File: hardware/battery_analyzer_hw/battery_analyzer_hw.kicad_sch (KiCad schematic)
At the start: 0 parts

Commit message: feat(hw): add USB-C with native JTAG and AMS1117-3.3 power block
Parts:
- added C1: 10uF, Package_SO:SOIC-8_3.9x4.9mm_P1.27mm, symbol Device:C_Polarized_Small
- added C2: 100nF, Package_TO_SOT_SMD:SOT-23-6, symbol Device:C_Small
- added C3: 22uF, symbol Device:C_Polarized_Small
- added C4: 100nF, symbol Device:C_Small
- added F1: Polyfuse 500mA, symbol Device:Polyfuse
- added J1: USB_C_Receptacle_USB2.0_16P, symbol Connector:USB_C_Receptacle_USB2.0_16P
- added R1: 5k1, Package_DIP:DIP-8_W7.62mm, symbol Device:R
- added R2: 5k1, symbol Device:R
- added U1: USBLC6-2SC6, Package_TO_SOT_SMD:SOT-23-6, symbol Power_Protection:USBLC6-2SC6
- added U2: AMS1117-3.3, Package_TO_SOT_SMD:SOT-223-3_TabPin2, symbol Regulator_Linear:AMS1117-3.3
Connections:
- new net: F1.2, J1.A4 (VBUS), J1.A9 (VBUS), J1.B4 (VBUS), J1.B9 (VBUS)
- new net: J1.A5 (CC1), R2.1
- new net: J1.A6 (D+), J1.B6 (D+), U1.3 (I/O2)
- new net: J1.A7 (D-), J1.B7 (D-), U1.1 (I/O1)
- new net: J1.B5 (CC2), R1.1
- new net +3.3V: C3.1, C4.1, U2.2 (VO)
- new net +5V: C1.1, C2.1, F1.1, U1.5 (VBUS), U2.3 (VI)
- new net GND: C1.2, C2.2, C3.2, C4.2, J1.A1 (GND), J1.A12 (GND), J1.B1 (GND), J1.B12 (GND), J1.SH (SHIELD), R1.2, R2.2, U1.2 (GND), U2.1 (GND)
- new net USB_D+: U1.4 (I/O2)
- new net USB_D-: U1.6 (I/O1)
- no-connect marks 0 -> 2

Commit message: feat(hw): add ESP32-S3 core, strapping pins and boot logic
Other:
- added sheet MCU_Core (mcu_core.kicad_sch)
- moved on the sheet: U1
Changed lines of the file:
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@@
 	(wire
 		(pts
-			(xy 113.03 60.96) (xy 123.19 60.96)
+			(xy 123.19 69.85) (xy 133.35 69.85)
 		)
 		(stroke
@@
 	(wire
 		(pts
-			(xy 113.03 58.42) (xy 123.19 58.42)
-		)
-		(stroke
-			(width 0)
-			(type default)
-		)
-	)
-	(wire
-		(pts
-			(xy 99.06 49.53) (xy 107.95 49.53)
+			(xy 123.19 67.31) (xy 133.35 67.31)
+		)
+		(stroke
+			(width 0)
+			(type default)
+		)
+	)
+	(wire
+		(pts
+			(xy 109.22 58.42) (xy 118.11 58.42)
 		)
 		(stroke
@@
 	(wire
 		(pts
-			(xy 76.2 55.88) (xy 76.2 58.42)
+			(xy 76.2 55.88) (xy 76.2 67.31)
 		)
 		(stroke
@@
 	(wire
 		(pts
-			(xy 72.39 60.96) (xy 102.87 60.96)
+			(xy 72.39 69.85) (xy 113.03 69.85)
 		)
 		(stroke
@@
 	(wire
 		(pts
-			(xy 76.2 58.42) (xy 102.87 58.42)
+			(xy 76.2 67.31) (xy 113.03 67.31)
 		)
 		(stroke
@@
 	(wire
 		(pts
-			(xy 107.95 49.53) (xy 107.95 53.34)
+			(xy 118.11 58.42) (xy 118.11 62.23)
 		)
 		(stroke
@@
 	(wire
 		(pts
+			(xy 72.39 69.85) (xy 72.39 60.96)
+		)
+		(stroke
+			(width 0)
+			(type default)
+		)
+	)
+	(wire
+		(pts
 			(xy 26.67 115.57) (xy 36.83 115.57)
 		)
@@
 	(wire
 		(pts
-			(xy 107.95 66.04) (xy 107.95 74.93)
+			(xy 118.11 74.93) (xy 118.11 83.82)
 		)
 		(stroke
@@
 	)
 	(label "USB_D-"
-		(at 123.19 58.42 0)
+		(at 133.35 67.31 0)
 		(effects
 			(font
@@
 	)
 	(label "+5V"
-		(at 96.52 40.64 0)
+		(at 104.14 40.64 0)
 		(effects
 			(font
@@
 	)
 	(label "USB_D+"
-		(at 123.19 60.96 0)
+		(at 133.35 69.85 0)
 		(effects
 			(font
@@
 	)
 	(label "+5V"
-		(at 31.75 115.57 0)
+		(at 26.67 115.57 0)
 		(effects
 			(font
@@
 	)
 	(label "+5V"
-		(at 99.06 49.53 0)
+		(at 109.22 58.42 0)
 		(effects
 			(font
@@
 	(symbol
 		(lib_id "power:GND")
-		(at 107.95 74.93 0)
+		(at 118.11 83.82 0)
 		(unit 1)
 		(body_style 1)
@@
 		(fields_autoplaced yes)
 		(property "Reference" "#PWR04"
-			(at 107.95 81.28 0)
+			(at 118.11 90.17 0)
 			(hide yes)
 			(show_name no)
@@
 		)
 		(property "Value" "GND"
-			(at 107.95 80.01 0)
+			(at 118.11 88.9 0)
 			(show_name no)
 			(do_not_autoplace no)
@@
 		)
 		(property "Footprint" ""
-			(at 107.95 74.93 0)
+			(at 118.11 83.82 0)
 			(hide yes)
 			(show_name no)
@@
 		)
 		(property "Datasheet" ""
-			(at 107.95 74.93 0)
+			(at 118.11 83.82 0)
 			(hide yes)
 			(show_name no)
@@
 		)
 		(property "Description" "Power symbol creates a global label with name \"GND\" , ground"
-			(at 107.95 74.93 0)
+			(at 118.11 83.82 0)
 			(hide yes)
 			(show_name no)
@@
 	(symbol
 		(lib_id "Power_Protection:USBLC6-2SC6")
-		(at 107.95 58.42 0)
+		(at 118.11 67.31 0)
 		(unit 1)
 		(body_style 1)
@@
 		(fields_autoplaced yes)
 		(property "Reference" "U1"
-			(at 109.6011 50.8 0)
+			(at 119.7611 59.69 0)
 			(show_name no)
 			(do_not_autoplace no)
@@
 		)
 		(property "Value" "USBLC6-2SC6"
-			(at 109.6011 53.34 0)
+			(at 119.7611 62.23 0)
 			(show_name no)
 			(do_not_autoplace no)
@@
 		)
 		(property "Footprint" "Package_TO_SOT_SMD:SOT-23-6"
-			(at 109.22 64.77 0)
+			(at 119.38 73.66 0)
 			(hide yes)
 			(show_name no)
@@
 		)
 		(property "Datasheet" "https://www.st.com/resource/en/datasheet/usblc6-2.pdf"
-			(at 109.22 66.675 0)
+			(at 119.38 75.565 0)
 			(hide yes)
 			(show_name no)
@@
 		)
 		(property "Description" "Very low capacitance ESD protection diode, 2 data-line, SOT-23-6"
-			(at 107.95 58.42 0)
+			(at 118.11 67.31 0)
 			(hide yes)
 			(show_name no)
@@
 				)
 			)
+		)
+	)
+	(sheet
+		(at -2.54 -257.81)
+		(size 311.15 218.44)
+		(exclude_from_sim no)
+		(in_bom yes)
+		(on_board yes)
+		(dnp no)
+		(fields_autoplaced yes)
+		(stroke
+			(width 0.1524)
+			(type solid)
+		)
+		(fill
+			(color 0 0 0 0)
+		)
+		(property "Sheetname" "MCU_Core"
+			(at -2.54 -258.5216 0)
+			(show_name no)
+			(do_not_autoplace no)
+			(effects
+				(font
+					(size 1.27 1.27)
+				)
+				(justify left bottom)
+			)
+		)
+		(property "Sheetfile" "mcu_core.kicad_sch"
+			(at -2.54 -38.7854 0)
+			(show_name no)
+			(do_not_autoplace no)
+			(effects
+				(font
+					(size 1.27 1.27)
+				)
+				(justify left top)
+			)
+		)
+		(instances
+			(project "battery_analyzer_hw"
+				(path "/1337d129-c752-45b4-85a9-21e5a5723565"
+					(page "2")
+				)
+			)

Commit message: feat(hw): add UI sheet with dual OLEDs, encoder and button
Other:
- added sheet UI_Controls (ui_controls.kicad_sch)
- moved on the sheet: C1, C2, C3, C4, F1, J1, R1, R2, U1, U2

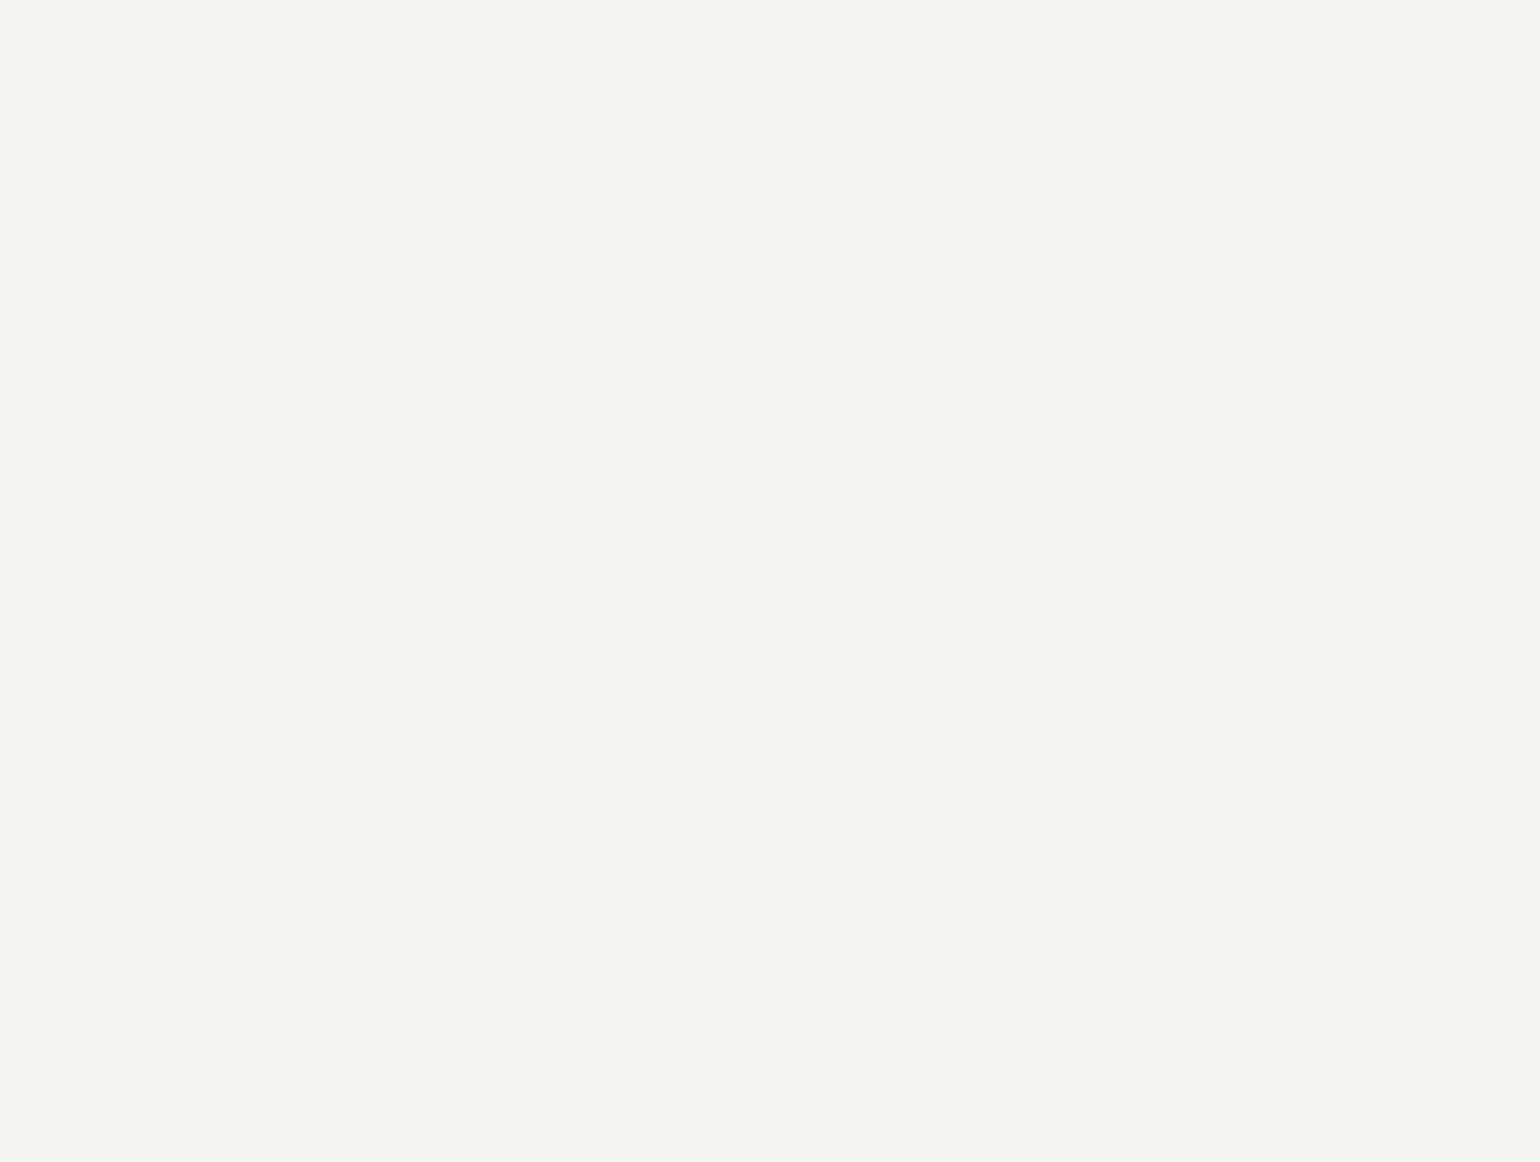
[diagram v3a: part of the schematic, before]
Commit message: feat(hw): add RJ45 slave ports, isolated 1-Wire and PWM routing fix(hw): split I2C into UI and PWR buses to prevent PID blocking
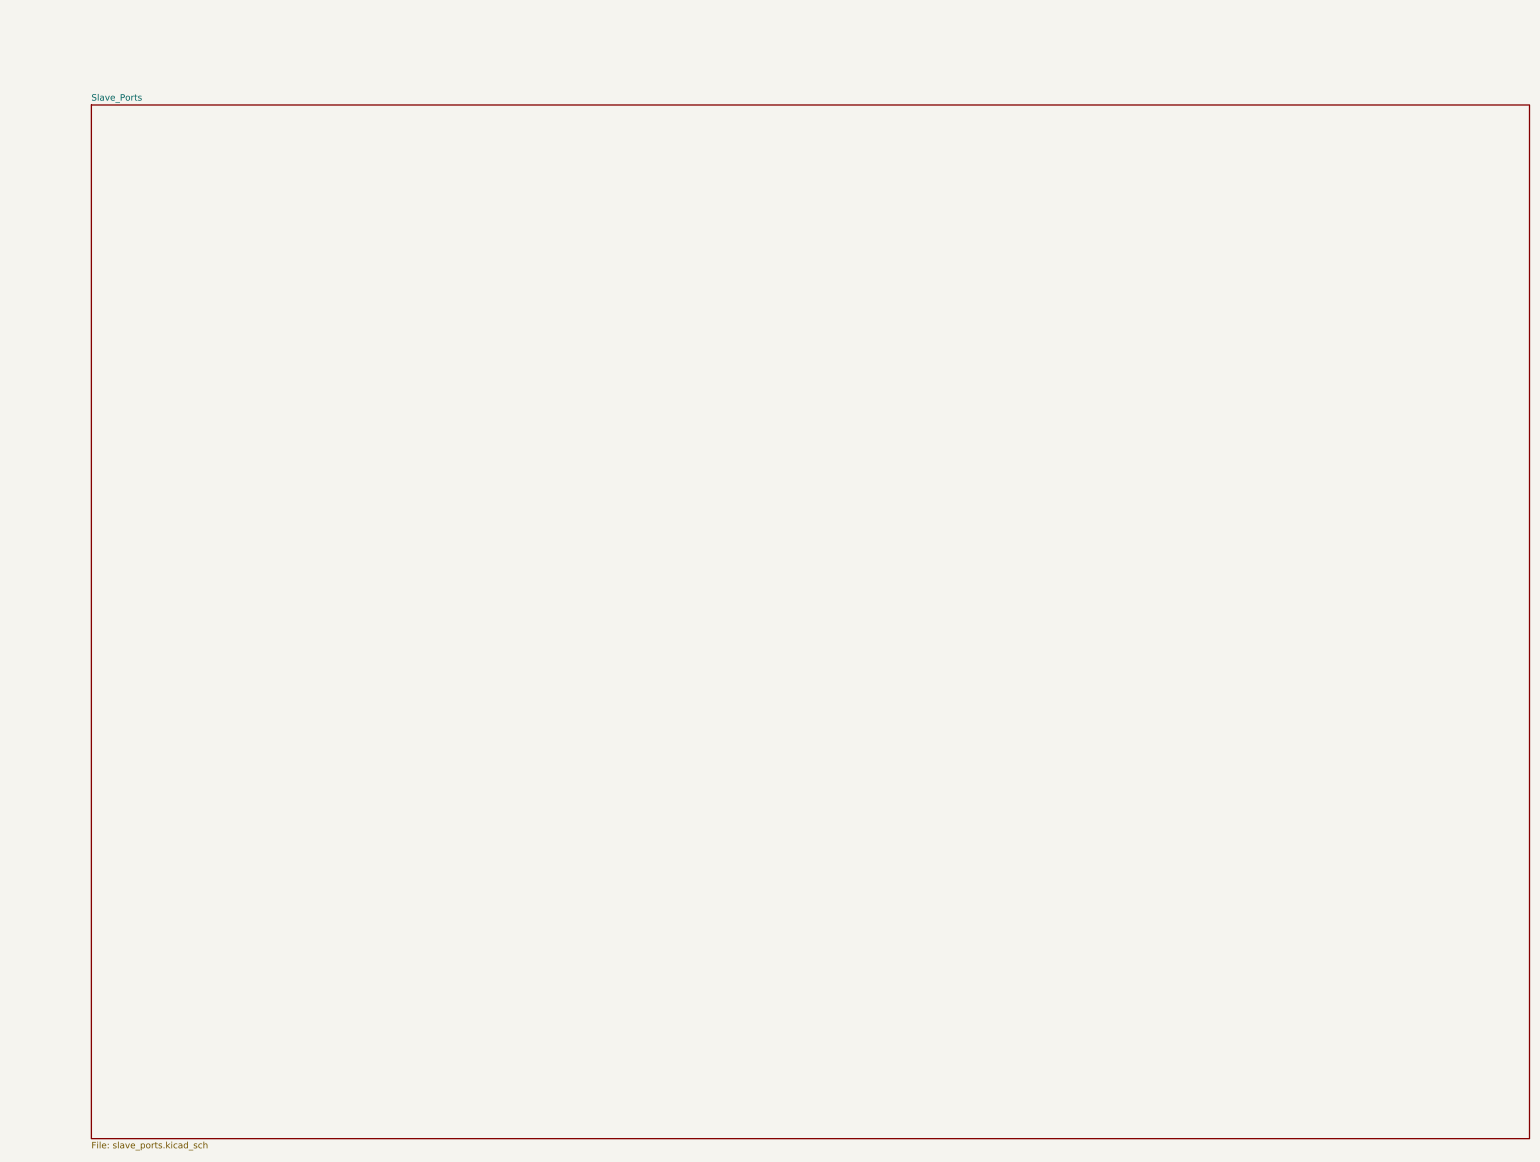
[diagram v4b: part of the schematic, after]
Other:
- added sheet Slave_Ports (slave_ports.kicad_sch)
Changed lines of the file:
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@@
+		)
+	)
+	(sheet
+		(at 359.41 -1.27)
+		(size 284.48 204.47)
+		(exclude_from_sim no)
+		(in_bom yes)
+		(on_board yes)
+		(dnp no)
+		(fields_autoplaced yes)
+		(stroke
+			(width 0.1524)
+			(type solid)
+		)
+		(fill
+			(color 0 0 0 0)
+		)
+		(property "Sheetname" "Slave_Ports"
+			(at 359.41 -1.9816 0)
+			(show_name no)
+			(do_not_autoplace no)
+			(effects
+				(font
+					(size 1.27 1.27)
+				)
+				(justify left bottom)
+			)
+		)
+		(property "Sheetfile" "slave_ports.kicad_sch"
+			(at 359.41 203.7846 0)
+			(show_name no)
+			(do_not_autoplace no)
+			(effects
+				(font
+					(size 1.27 1.27)
+				)
+				(justify left top)
+			)
+		)
+		(instances
+			(project "battery_analyzer_hw"
+				(path "/1337d129-c752-45b4-85a9-21e5a5723565"
+					(page "4")
+				)
+			)
 		)
 	)

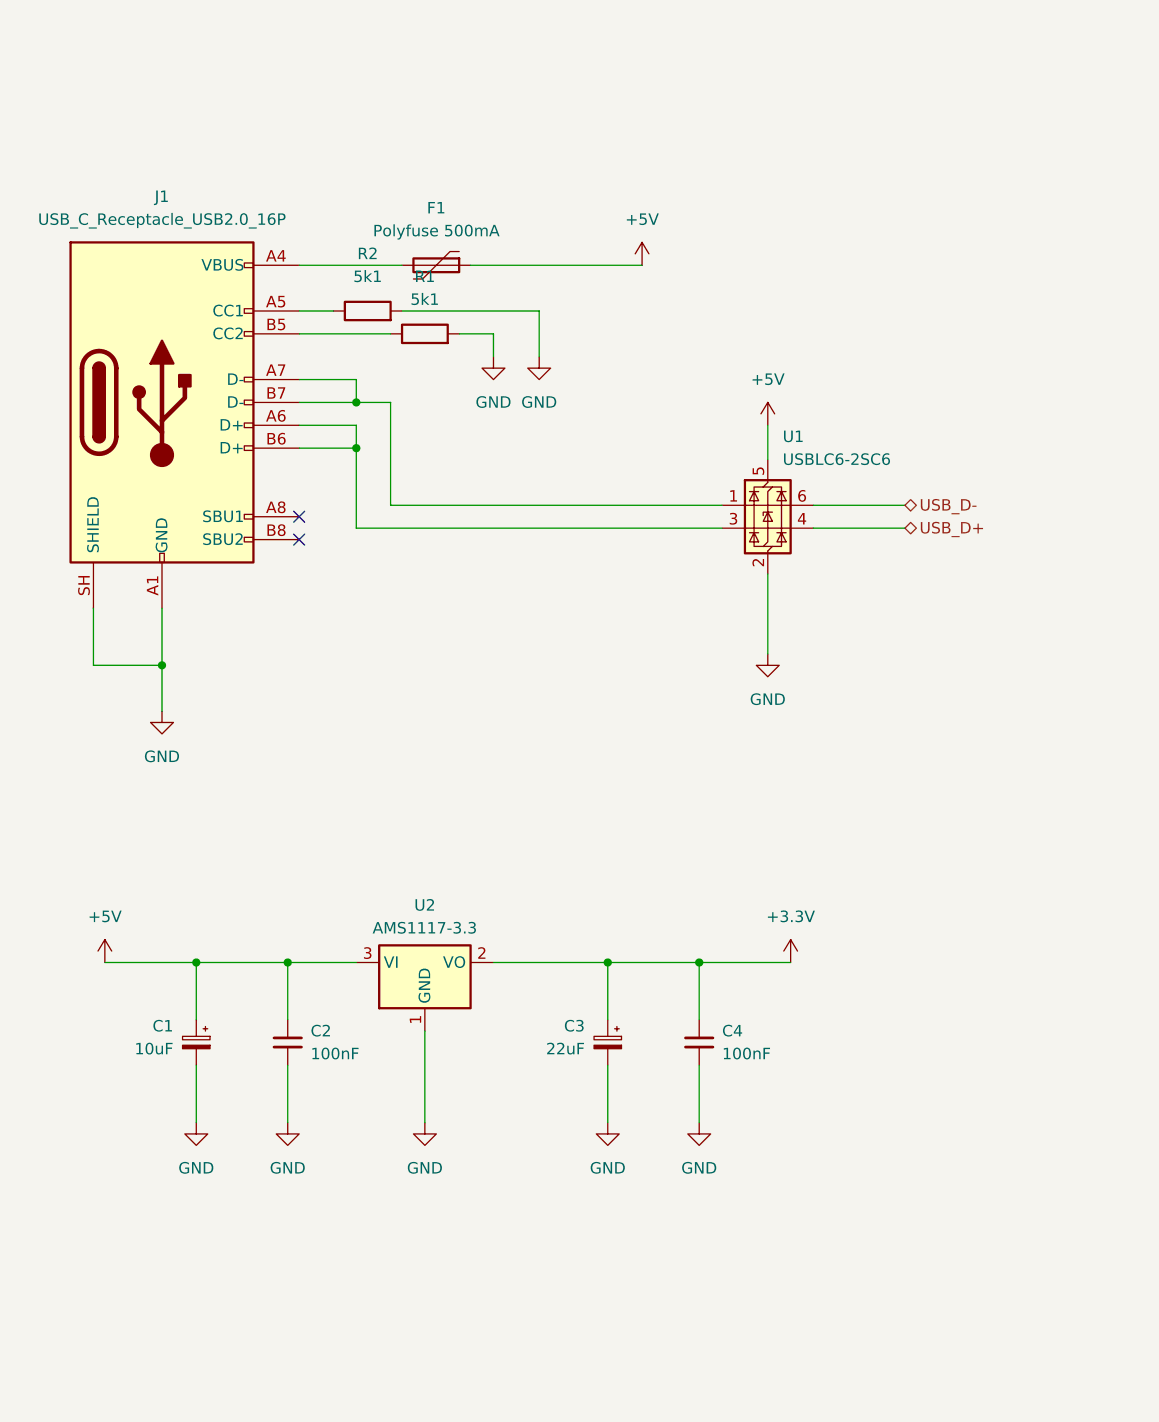
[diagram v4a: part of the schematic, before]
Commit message: hw(master): fix footprints, apply HandSolder and Tantalum
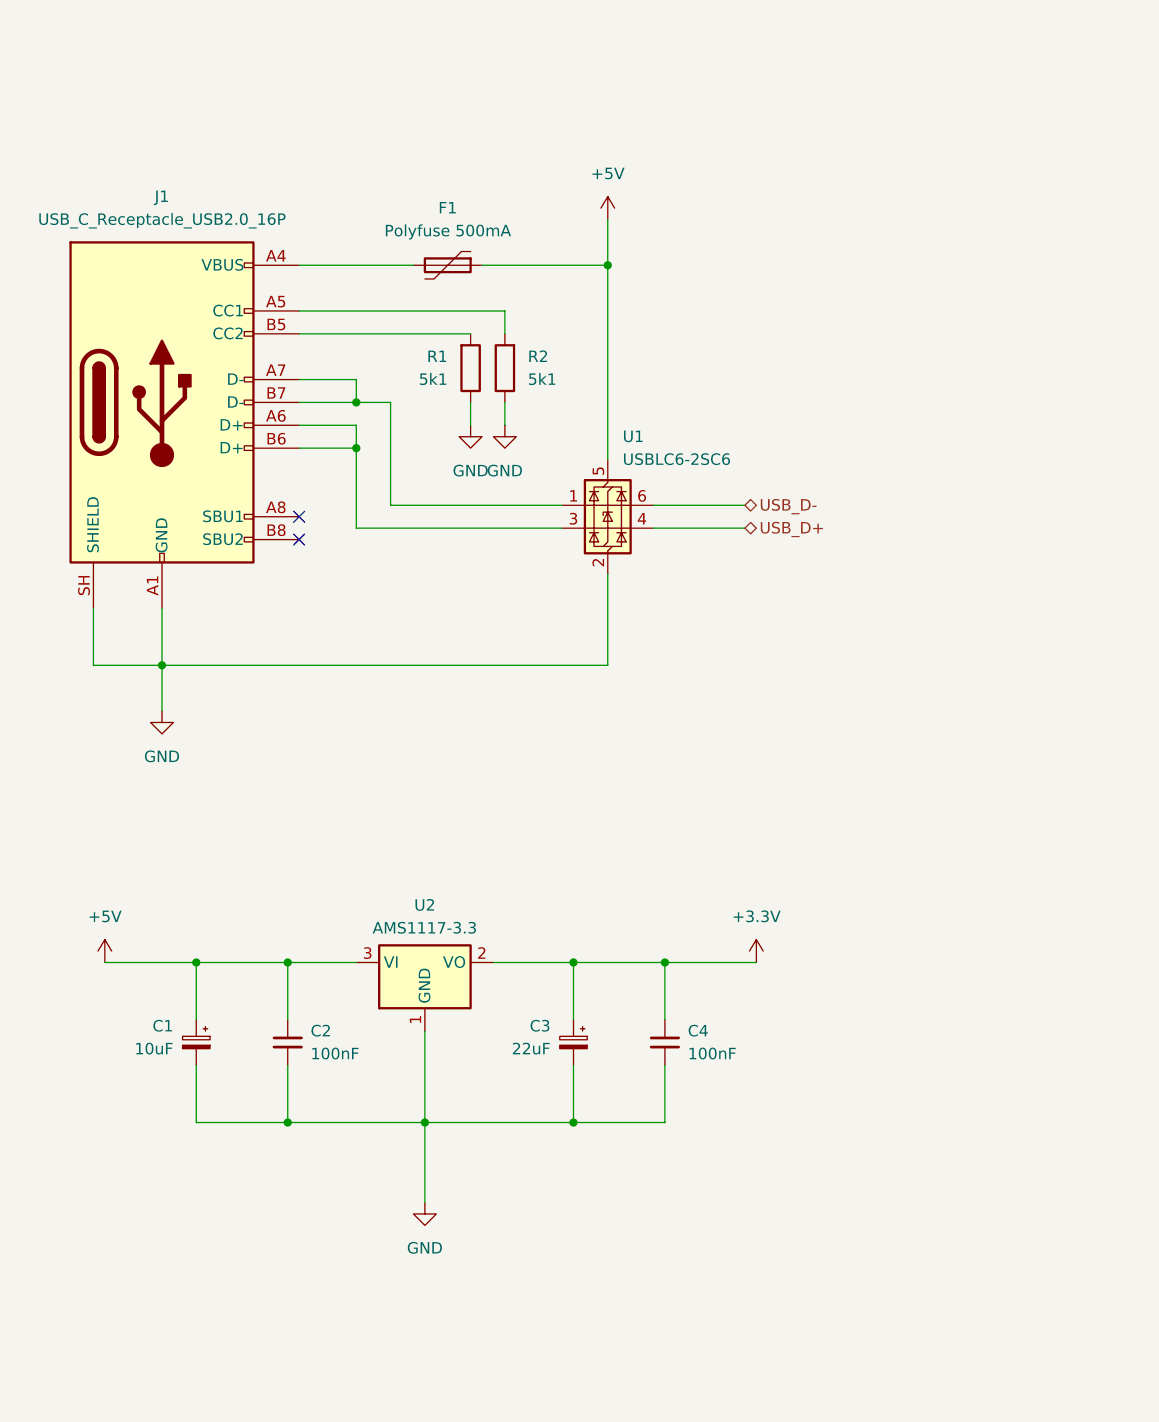
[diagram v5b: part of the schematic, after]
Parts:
- C1: footprint Package_SO:SOIC-8_3.9x4.9mm_P1.27mm -> Capacitor_Tantalum_SMD:CP_EIA-3216-18_Kemet-A_HandSolder
- C2: footprint Package_TO_SOT_SMD:SOT-23-6 -> Capacitor_SMD:C_0805_2012Metric_Pad1.18x1.45mm_HandSolder
- C3: footprint (none) -> Capacitor_Tantalum_SMD:CP_EIA-3528-21_Kemet-B_HandSolder
- C4: footprint (none) -> Capacitor_SMD:C_0805_2012Metric_Pad1.18x1.45mm_HandSolder
- F1: footprint (none) -> Fuse:Fuse_1206_3216Metric_Pad1.42x1.75mm_HandSolder
- J1: footprint (none) -> Connector_USB:USB_C_Receptacle_HRO_TYPE-C-31-M-12
- R1: footprint Package_DIP:DIP-8_W7.62mm -> Resistor_SMD:R_0805_2012Metric_Pad1.20x1.40mm_HandSolder
- R2: footprint (none) -> Resistor_SMD:R_0805_2012Metric_Pad1.20x1.40mm_HandSolder
- U1: footprint Package_TO_SOT_SMD:SOT-23-6 -> Package_TO_SOT_SMD:SOT-23-6_Handsoldering
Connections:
- net GND: now also R1.1, R2.1; no longer R1.2, R2.2
- net at J1.A5 (CC1): now also R2.2; no longer R2.1
- net at J1.B5 (CC2): now also R1.2; no longer R1.1
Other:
- moved on the sheet: C3, C4, F1, R1, U1
